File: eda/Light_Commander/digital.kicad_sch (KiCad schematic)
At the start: 1 part, among them U1 STM32F446RETx

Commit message: Power and UI on PCB
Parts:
- added D1, D2, D3, D4: GSBAT54W, Diode_SMD:D_SOD-123, symbol Device:D_Schottky
- added Q1, Q2, Q3, Q4: MMBT3904, Package_TO_SOT_SMD:SOT-23, symbol Transistor_BJT:MMBT3904
- added R25, R27, R29, R30: 100k, Resistor_SMD:R_0805_2012Metric, symbol Device:R_US
- added R26, R28, R31, R32: 10k, Resistor_SMD:R_0805_2012Metric, symbol Device:R_US
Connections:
- net GATE2_EXTI: now reaches U1.10 (PC2)
- net GATE2_EXTI: now also Q4.3 (C), R32.2
- net GATE3_EXTI: now reaches U1.11 (PC3)
- net GATE3_EXTI: now also Q3.3 (C), R31.2
- net ENC_CH1: now reaches U1.41 (PA8)
- net ENC_CH2: now reaches U1.42 (PA9)
- net ENC_BTN: now reaches U1.56 (PB4)
- net GATE0_EXTI: now reaches U1.8 (PC0)
- net GATE0_EXTI: now also Q1.3 (C), R26.2
- net GATE1_EXTI: now reaches U1.9 (PC1)
- net GATE1_EXTI: now also Q2.3 (C), R28.2
- new net: D1.1 (K), Q1.1 (B), R25.2
- new net: D4.1 (K), Q4.1 (B), R30.2
- new net: D2.1 (K), Q2.1 (B), R27.2
- new net: D3.1 (K), Q3.1 (B), R29.2
- new net +3V3: R26.1, R28.1, R31.1, R32.1
- new net GATE0_JACK: R25.1
- new net GATE1_JACK: R27.1
- new net GATE2_JACK: R30.1
- new net GATE3_JACK: R29.1
- new net GND: D1.2 (A), D2.2 (A), D3.2 (A), D4.2 (A), Q1.2 (E), Q2.2 (E), Q3.2 (E), Q4.2 (E)
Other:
- moved on the sheet: U1

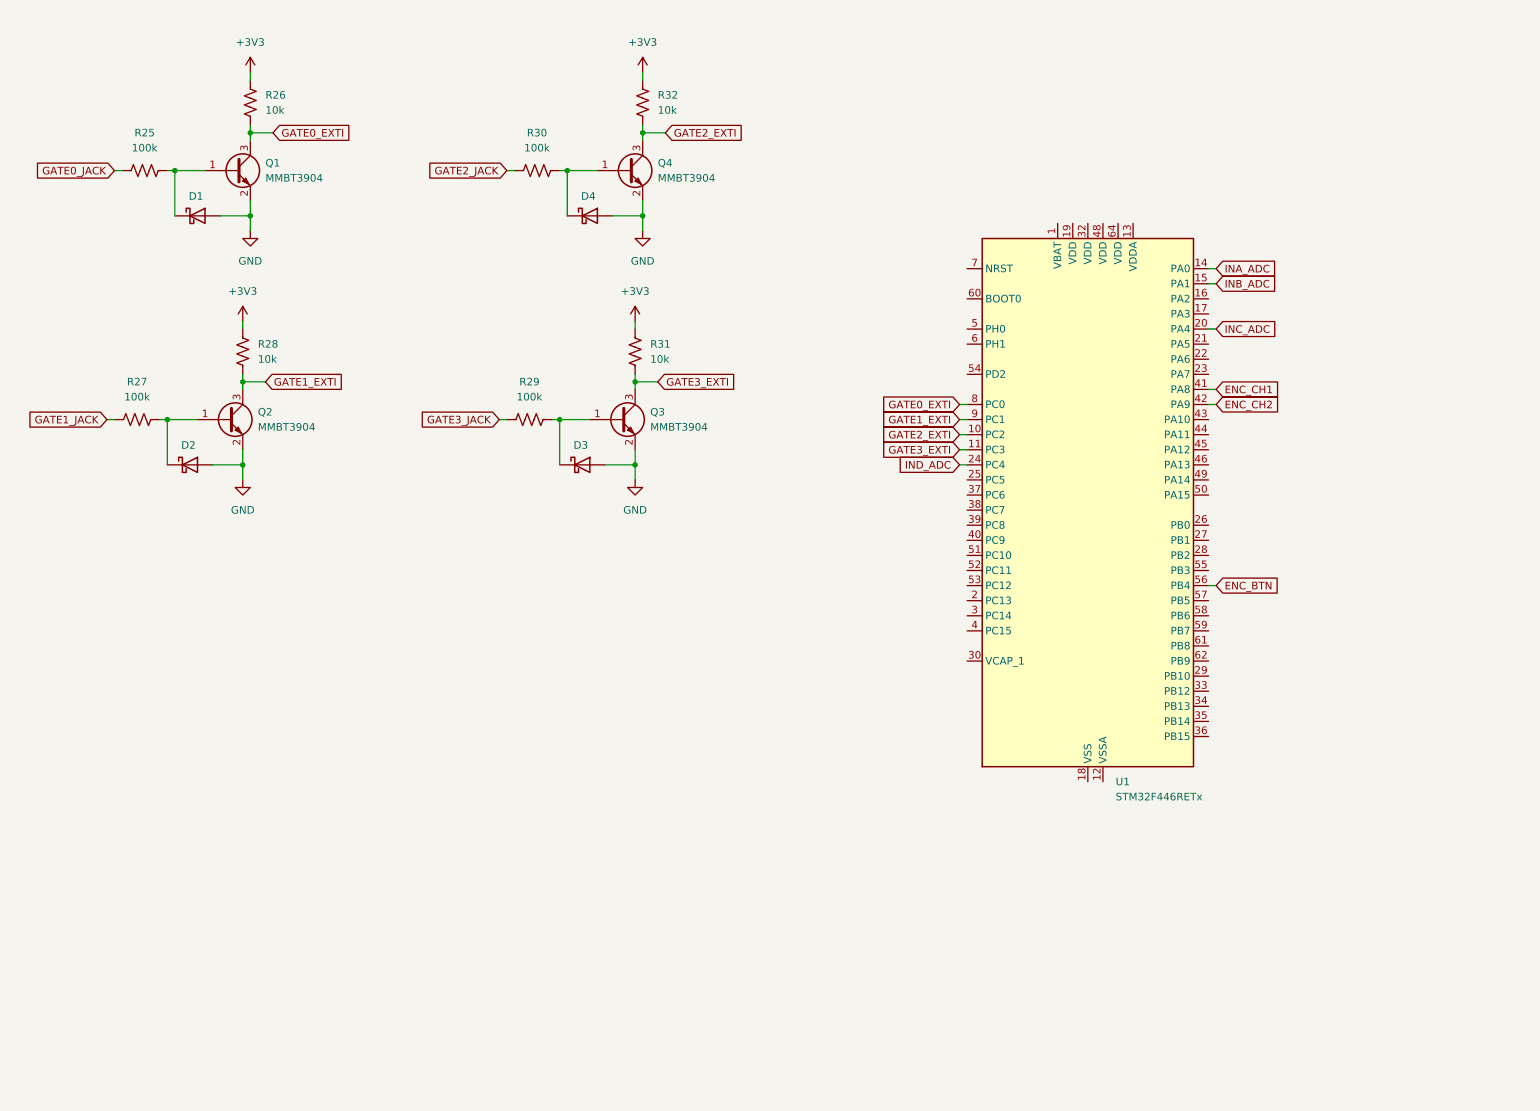
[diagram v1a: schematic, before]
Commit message: Voltage ref, BOOT0, and connections on PCB
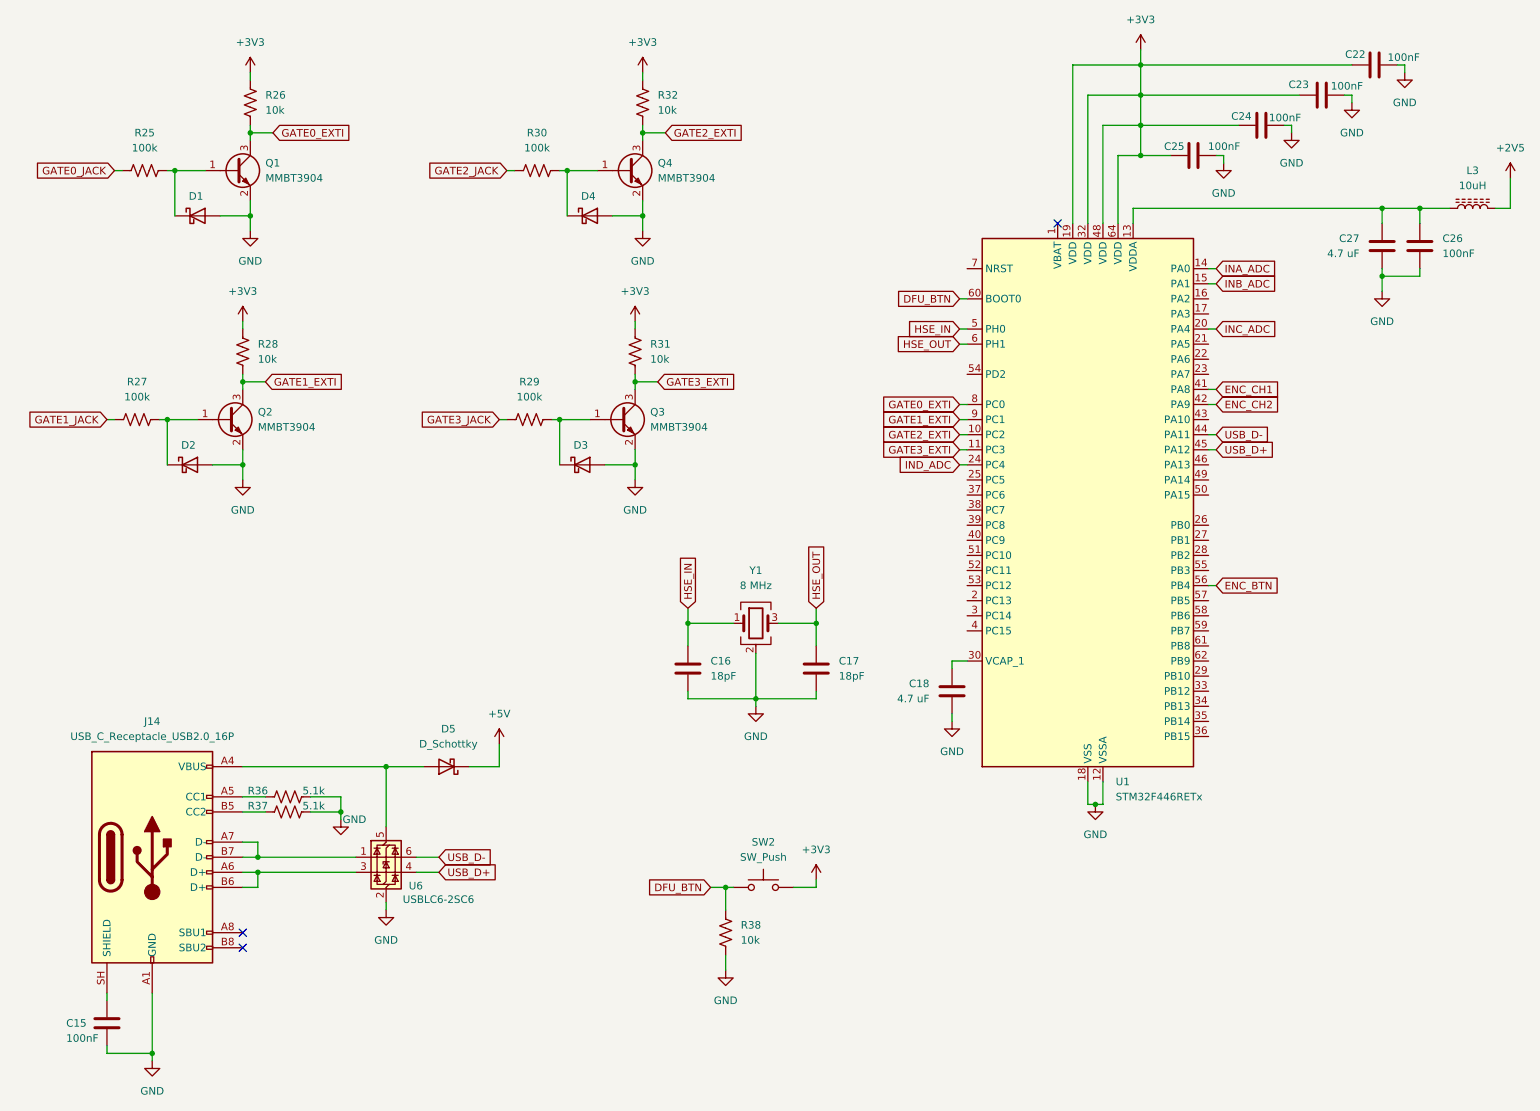
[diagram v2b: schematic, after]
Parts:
- added C15, C22, C23, C24, C25, C26: 100nF, Capacitor_SMD:C_0805_2012Metric, symbol Device:C
- added C16, C17: 18pF, Capacitor_SMD:C_0402_1005Metric, symbol Device:C
- added C18, C27: 4.7 uF, Capacitor_SMD:C_0805_2012Metric, symbol Device:C
- added D5: D_Schottky, Diode_SMD:D_SOD-123, symbol Device:D_Schottky
- added J14: USB_C_Receptacle_USB2.0_16P, footprints:UJ20-C-H-G-SMT-1-P16-TR, symbol Connector:USB_C_Receptacle_USB2.0_16P
- added L3: 10uH, Inductor_SMD:L_1210_3225Metric, symbol Device:L_Ferrite
- added R36, R37: 5.1k, Resistor_SMD:R_0805_2012Metric, symbol Device:R_US
- added R38: 10k, Resistor_SMD:R_0805_2012Metric, symbol Device:R_US
- added SW2: SW_Push, footprints:TS09-63-25-R-160-SMT-TR, symbol Switch:SW_Push
- added U6: USBLC6-2SC6, Package_TO_SOT_SMD:SOT-23-6, symbol Power_Protection:USBLC6-2SC6
- added Y1: 8 MHz, footprints:ECS-80-18-33-JGN-TR, symbol Device:Crystal_GND24
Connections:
- net +3V3: now also U1.19 (VDD), U1.32 (VDD), U1.48 (VDD), U1.64 (VDD), C22.2, C23.1, C24.1, C25.2, SW2.2
- net GND: now also U1.12 (VSSA), U1.18 (VSS), U1.31 (VSS), U1.47 (VSS), U1.63 (VSS), C15.2, C16.2, C17.2, C18.1, C22.1, C23.2, C24.2, C25.1, C26.1, C27.1, J14.A1 (GND), J14.A12 (GND), J14.B1 (GND), J14.B12 (GND), R36.1, R37.1, R38.2, U6.2 (GND), Y1.2 (G), Y1.4 (G)
- net at U1.13 (VDDA): now also C26.2, C27.2, L3.1
- net at U1.30 (VCAP_1): now also C18.2
- net USB_D-: now reaches U1.44 (PA11)
- net USB_D-: now also U6.6 (I/O1)
- net USB_D+: now reaches U1.45 (PA12)
- net USB_D+: now also U6.4 (I/O2)
- net HSE_IN: now reaches U1.5 (PH0)
- net HSE_IN: now also C16.1, Y1.1
- net HSE_OUT: now reaches U1.6 (PH1)
- net HSE_OUT: now also C17.1, Y1.3
- net DFU_BTN: now reaches U1.60 (BOOT0)
- net DFU_BTN: now also R38.1, SW2.1
- new net: J14.A5 (CC1), R36.2
- new net: D5.2 (A), J14.A4 (VBUS), J14.A9 (VBUS), J14.B4 (VBUS), J14.B9 (VBUS), U6.5 (VBUS)
- new net: J14.A6 (D+), J14.B6 (D+), U6.3 (I/O2)
- new net: J14.A7 (D-), J14.B7 (D-), U6.1 (I/O1)
- new net: J14.B5 (CC2), R37.2
- new net: C15.1, J14.SH (SHIELD)
- new net +2V5: L3.2
- new net +5V: D5.1 (K)
- no-connect marks 0 -> 3
